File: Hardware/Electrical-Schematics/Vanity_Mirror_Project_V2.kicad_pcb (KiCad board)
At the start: 2 copper layers, 76.9 x 51.2 mm, 41 parts, among them IC1 SN74LV1T34QDBVRQ1, IC2 FDC1004QDGSRQ1, J1 USB_C_Receptacle_USB2.0_14P, Q1 Q_NPN_BEC, Q2 Q_NPN_BEC, SW1 RST, U1 CH340C, U2 ESP-12F, U3 USBLC6-2SC6, U4 XL1509-3.3

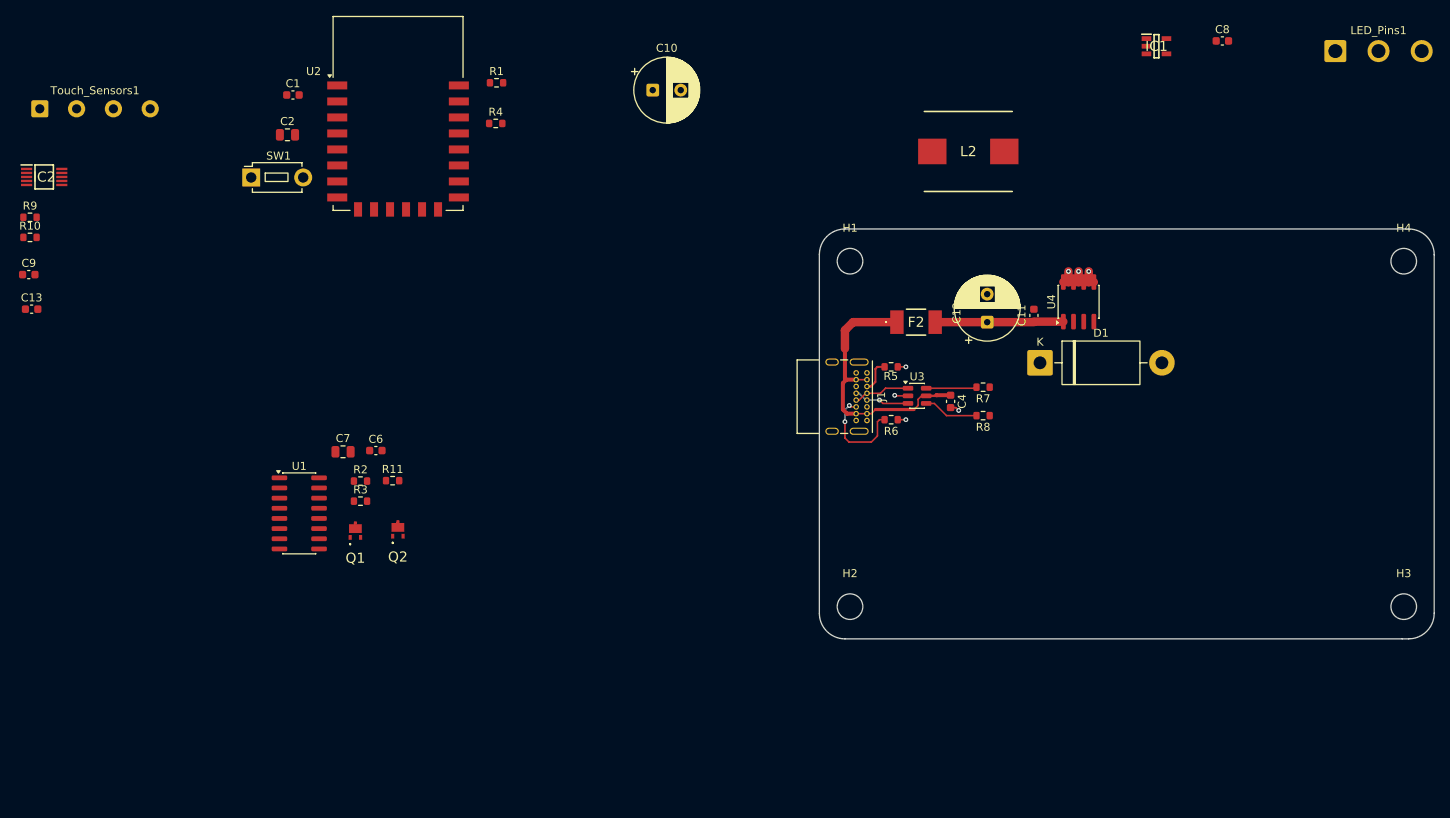
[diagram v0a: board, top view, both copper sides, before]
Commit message: 2nd version of the design
Changed multiple footprints to smd parts, Made a 2nd version for the PCB utilizing a power plane. PCB is ready to be manufactured
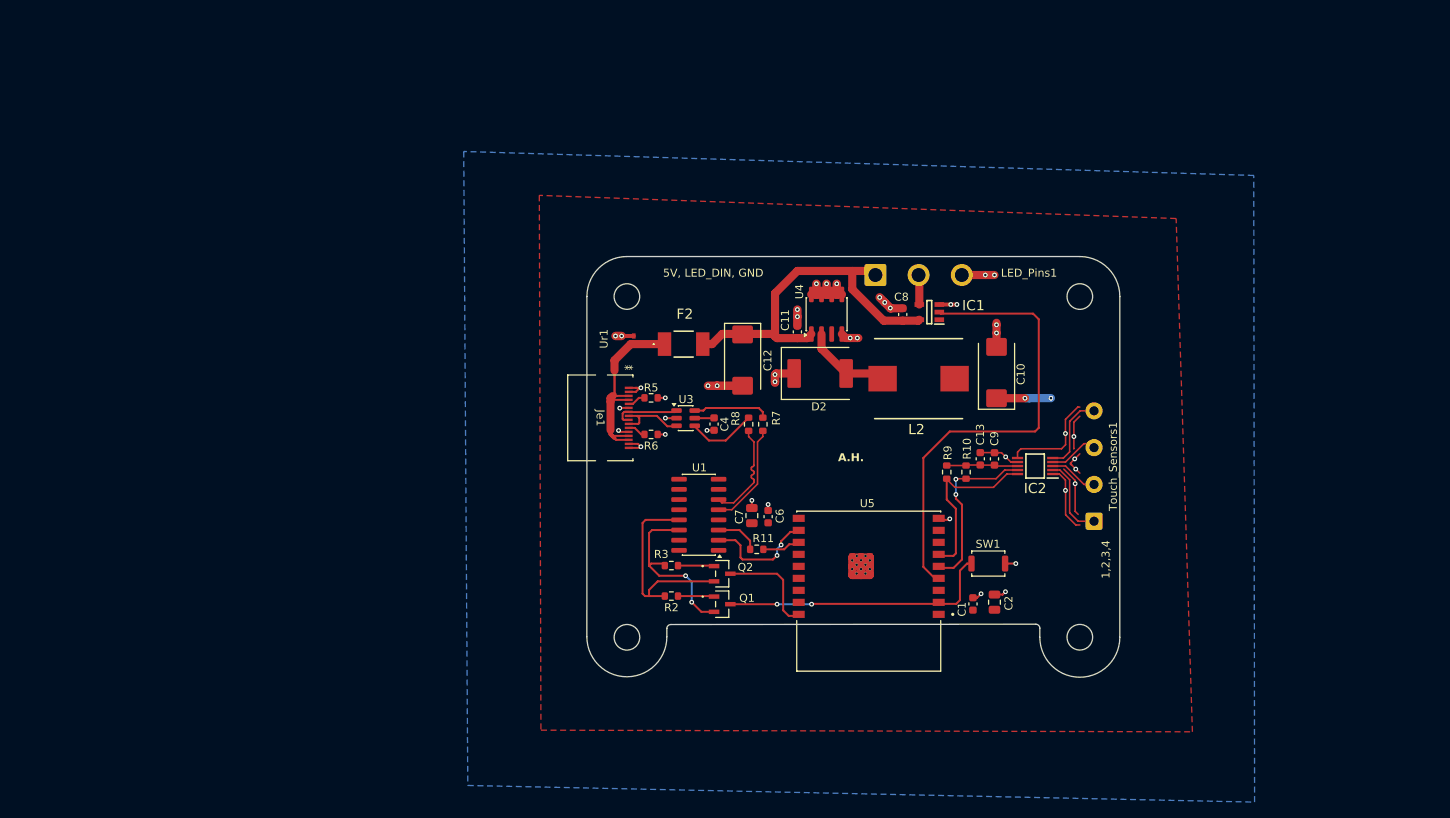
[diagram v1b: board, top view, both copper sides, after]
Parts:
- removed D1: 1N5820, Diode_THT:D_DO-201AD_P15.24mm_Horizontal
- removed J1: USB_C_Receptacle_USB2.0_14P, Connector_USB:USB_C_Receptacle_GCT_USB4085
- removed R1, R4: 10k, Resistor_SMD:R_0603_1608Metric
- removed U2: ESP-12F, RF_Module:ESP-12E
- added D2: Diode, VanityMirror_FootPrints:P27_DO-214AB_SMC, F.Cu at (135.9, 73.7)
- added Je1: 10155435-00011LF-Custom, VanityMirror_FootPrints:2130830005_MOL, F.Cu at (111.7, 79.3)
- added U5: ESP32-C3-WROOM-02-N4, VanityMirror_FootPrints:MODULE_ESP32-C3-WROOM-02-H4, F.Cu at (145.2, 100.9)
- added Ur1: CPDQR5V0U, VanityMirror_FootPrints:CPDQR, F.Cu at (115.8, 69.5)
- C10: value 470uF -> 330uF; footprint Capacitor_THT:CP_Radial_D8.0mm_P3.50mm -> Capacitor_Tantalum_SMD:CP_EIA-7343-31_Kemet-D_HandSolder
- C12: footprint Capacitor_THT:CP_Radial_D8.0mm_P3.50mm -> Capacitor_Tantalum_SMD:CP_EIA-7343-31_Kemet-D_HandSolder
- Q1, Q2: footprint VanityMirror_FootPrints:PMEG2020EPASX -> VanityMirror_FootPrints:SOT-23-3_1P4X3P040_ONS
- R11: value 10k -> 499
- SW1: footprint Button_Switch_THT:SW_PUSH_1P1T_6x3.5mm_H4.3_APEM_MJTP1243 -> Button_Switch_SMD:SW_Push_SPST_NO_Alps_SKRK
- moved Touch_Sensors1 141.5 mm to (173.4, 92.2), turned to 90 degrees
- moved IC2 129.0 mm to (166.0, 85.3), turned to 180 degrees
- moved C9 122.9 mm to (160.9, 84.4), turned to 90 degrees
- moved R10 120.6 mm to (157.4, 86.1), turned to 90 degrees
- moved C13 120.0 mm to (159.2, 84.4), turned to 90 degrees
- moved R9 118.9 mm to (155.0, 86.1), turned to 90 degrees
- moved C1 106.2 mm to (158.2, 102.5), turned to 90 degrees
- moved C2 105.9 mm to (160.9, 102.3), turned to 90 degrees
- moved SW1 104.0 mm to (160.2, 97.5), turned to 180 degrees
- moved LED_Pins1 63.9 mm to (146.0, 61.4)
- moved C10 55.6 mm to (161.2, 73.6), turned to 90 degrees
- moved C8 52.6 mm to (149.5, 66.4), turned to 90 degrees
- moved C7 51.7 mm to (130.6, 91.5), turned to 90 degrees
- moved U1 49.9 mm to (124.0, 91.4), turned to 180 degrees
- moved C6 49.7 mm to (132.6, 91.6), turned to 90 degrees
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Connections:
- net /~{RST} renamed /EN
- R11 pad 1: +3.3V -> Net-(U5-TXD)
- R11 pad 2: /GPIO0 -> /TX
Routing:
- net GND: track 12.7 -> 111.1 mm, vias 7 -> 43
- net /SN74_1A: track 0.00 -> 58.6 mm
- net /EN: track 0.00 -> 34.4 mm, vias 0 -> 2
- net +5V: track 16.0 -> 46.2 mm
- net Net-(Q2-E): track 0.00 -> 25.8 mm
- net Net-(Q1-E): track 0.00 -> 22.2 mm, vias 0 -> 2
- net /SDA: track 0.00 -> 22.1 mm
- net /SCL: track 0.00 -> 21.9 mm, vias 0 -> 2
- net +3.3V: track 0.00 -> 15.7 mm, vias 0 -> 2
- net /RX: track 0.00 -> 14.1 mm, vias 0 -> 2
- net /D+: track 0.00 -> 13.1 mm
- net /D-: track 0.00 -> 13.0 mm
- net /GPIO0: track 0.00 -> 13.0 mm
- net Net-(D2-C): track 0.00 -> 11.0 mm
- net Net-(Je1-CC2): track 12.7 -> 2.31 mm, vias 2 -> 0
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- added copper zone on F.Cu, net +3.3V
- added copper zone on B.Cu, net GND
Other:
- board size 76.9 x 51.2 mm -> 66.6 x 52.6 mm
- board text added: "1,2,3,4"
- board text added: "5V, LED_DIN, GND"
- board text added: "A.H."
- board text added: "U3"
